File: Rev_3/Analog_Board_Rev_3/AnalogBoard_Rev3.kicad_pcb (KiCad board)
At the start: 4 copper layers, 59.5 x 114.5 mm, 56 parts, among them J1 Conn_01x06_Male, J2 Conn_01x10_Male, J3 Conn_01x06_Male, J4 Conn_01x08_Male, SW1 SW_DIP_x04, U1 OPA2134, U12 NSL-32, U13 NSL-32, U2 OPA2134, U3 OPA2134, U4 OPA2134, U5 OPA2134, U6 NSL-32, U7 NSL-32, U8 NSL-32, U9 NSL-32

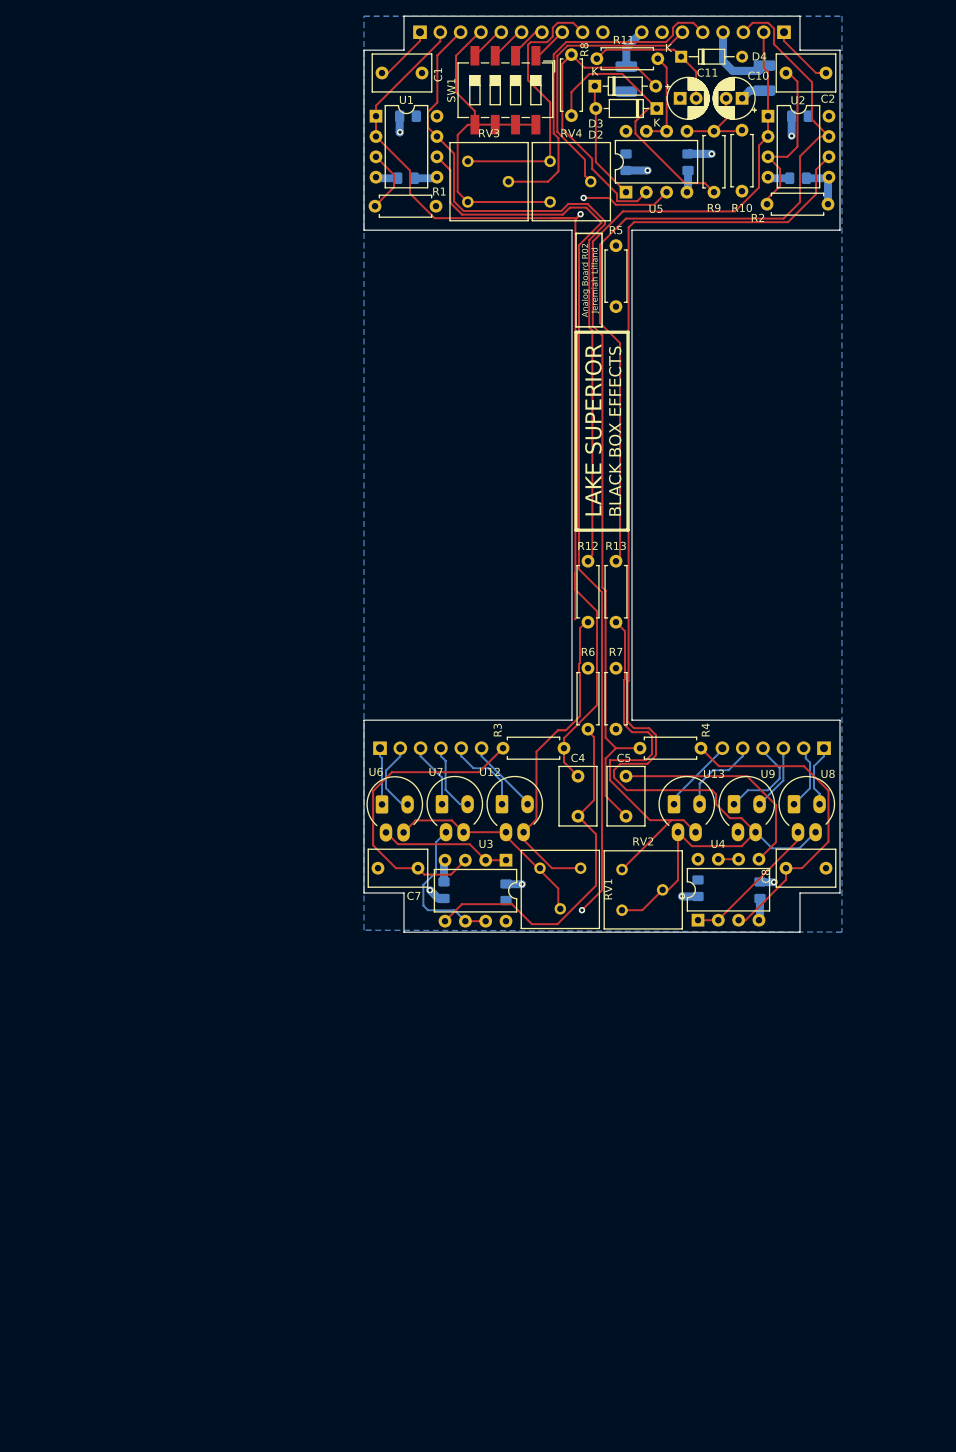
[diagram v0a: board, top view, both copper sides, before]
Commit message: Pivoting to Passive Jack Boards
Finalized layout for input/output Jack Boards, which are now completely passive and connected with board-to-board connectors. Schematics are not updated yet, just figuring out placement/dimensions.
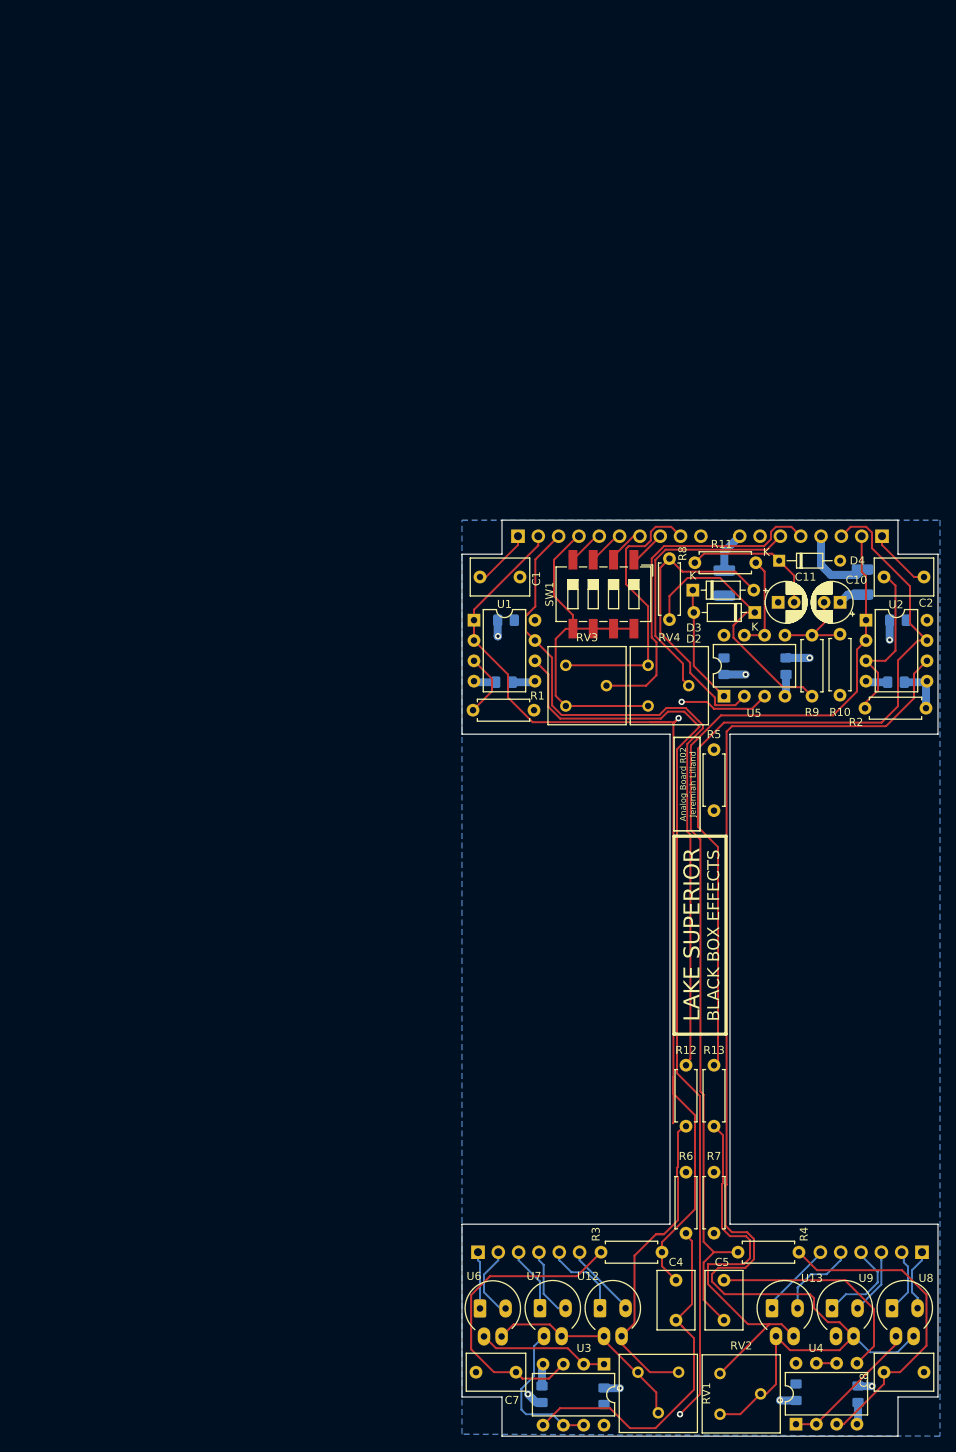
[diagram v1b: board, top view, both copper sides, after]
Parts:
- moved C10 64.2 mm to (148.3, 111.8)
- moved C11 64.2 mm to (140.5, 111.8)
- moved C12 64.2 mm to (155.2, 121.8)
- moved C13 64.2 mm to (118.8, 211.0)
- moved C14 64.2 mm to (111.0, 210.8)
- moved C15 64.2 mm to (142.8, 210.5)
- moved C16 64.2 mm to (150.5, 210.8)
- moved C17 64.2 mm to (133.8, 119.8)
- moved C18 64.2 mm to (141.5, 119.8)
- moved C19 64.2 mm to (133.8, 109.4)
- moved C3 64.2 mm to (106.5, 114.0)
- moved C4 64.2 mm to (127.8, 201.5)
- moved C5 64.2 mm to (133.8, 196.5)
- moved C6 64.2 mm to (106.2, 121.8)
- moved C7 64.2 mm to (102.8, 208.0)
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
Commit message: Added analog board back, switched to Jacks on Bottom
Added analog board mezzanine back to fit everything. Finalized decision on jack boards; jacks on bottom, wire to board connectors between jack boards and digital board. Tentative board outlines defined and scoped out component placement.
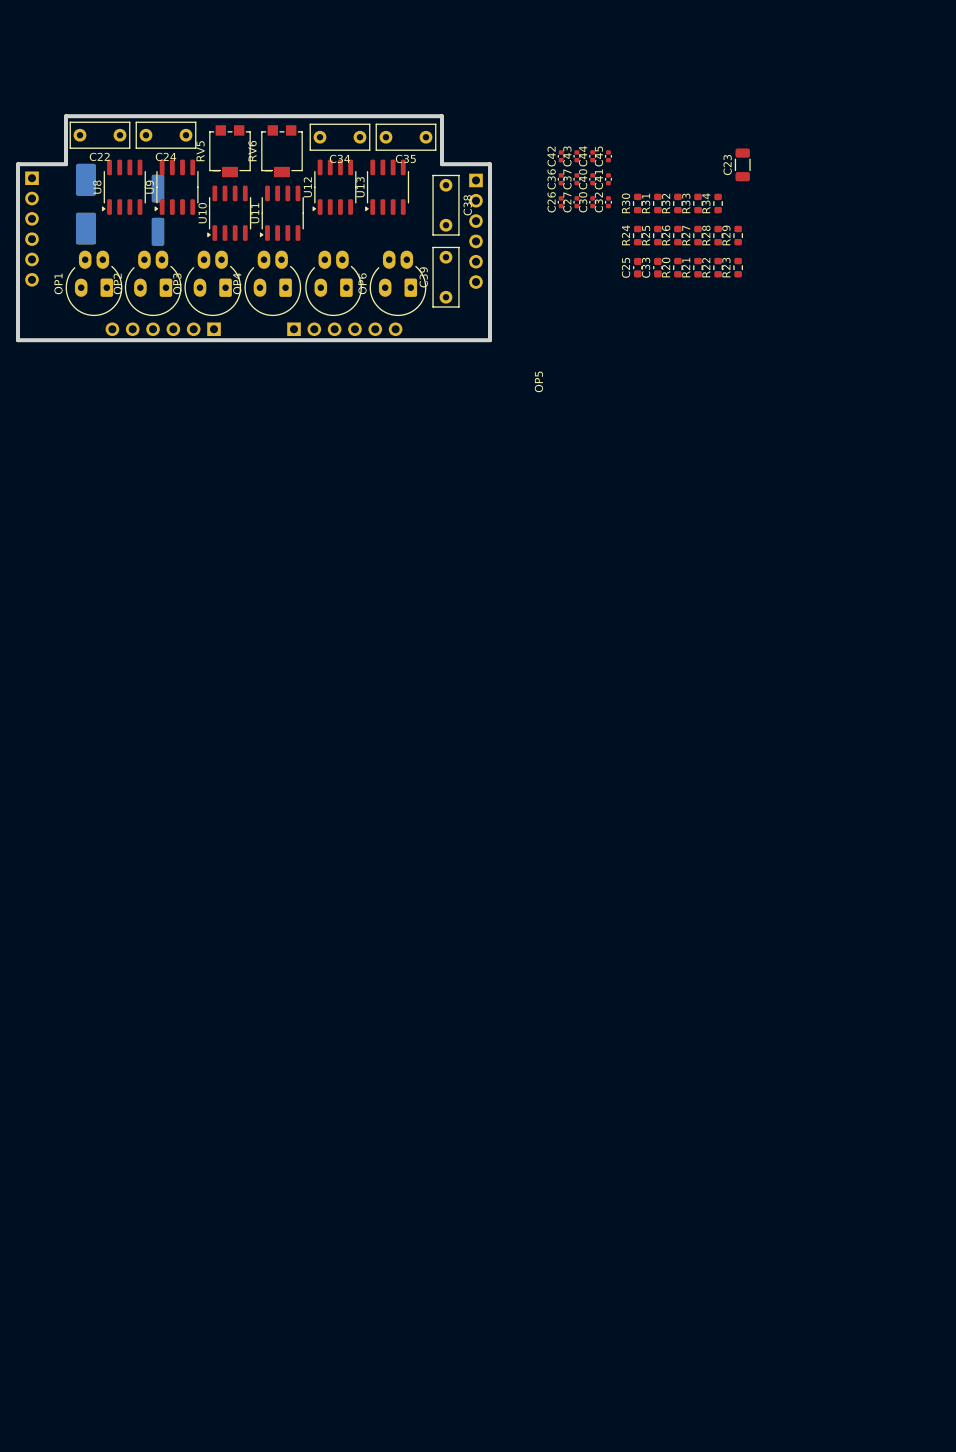
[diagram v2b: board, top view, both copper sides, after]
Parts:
- removed C1, C2: 47n, Capacitor_THT:C_Rect_L7.2mm_W4.5mm_P5.00mm_FKS2_FKP2_MKS2_MKP2
- removed C10: 4.7u, Capacitor_THT:CP_Radial_D5.0mm_P2.00mm
- removed C11: 47u, Capacitor_THT:CP_Radial_D5.0mm_P2.00mm
- removed C12, C13, C14, C15, C16, C17, C18, C3, C6, C9: 100n, Capacitor_SMD:C_0805_2012Metric_Pad1.18x1.45mm_HandSolder
- removed C19, C20: 10u, Capacitor_SMD:C_1210_3225Metric_Pad1.33x2.70mm_HandSolder
- removed C4, C5, C7, C8: 1n, Capacitor_THT:C_Rect_L7.2mm_W4.5mm_P5.00mm_FKS2_FKP2_MKS2_MKP2
- removed D2, D3: 1N914, Diode_THT:D_DO-35_SOD27_P7.62mm_Horizontal
- removed D4: D_Zener, Diode_THT:D_DO-34_SOD68_P7.62mm_Horizontal
- removed J1: Conn_01x06_Male, Connector_PinHeader_2.54mm:PinHeader_1x06_P2.54mm_Vertical
- removed J2: Conn_01x10_Male, Connector_PinHeader_2.54mm:PinHeader_1x10_P2.54mm_Vertical
- removed the J3 at (158.5, 193.0)
- removed J4: Conn_01x08_Male, Connector_PinHeader_2.54mm:PinHeader_1x08_P2.54mm_Vertical
- removed R1, R2: 1M, Resistor_THT:R_Axial_DIN0207_L6.3mm_D2.5mm_P7.62mm_Horizontal
- removed R10: 47k, Resistor_THT:R_Axial_DIN0207_L6.3mm_D2.5mm_P7.62mm_Horizontal
- removed R11, R12, R13: 1k, Resistor_THT:R_Axial_DIN0207_L6.3mm_D2.5mm_P7.62mm_Horizontal
- removed R3, R4, R6, R7: 470k, Resistor_THT:R_Axial_DIN0207_L6.3mm_D2.5mm_P7.62mm_Horizontal
- removed R5: 3.3k, Resistor_THT:R_Axial_DIN0207_L6.3mm_D2.5mm_P7.62mm_Horizontal
- removed R8: 100k, Resistor_THT:R_Axial_DIN0207_L6.3mm_D2.5mm_P7.62mm_Horizontal
- removed R9: 10k, Resistor_THT:R_Axial_DIN0207_L6.3mm_D2.5mm_P7.62mm_Horizontal
- removed RV1, RV2, RV3, RV4: 50k, Pinebox:Potentiometer_Bourns_3386F_Vertical
- removed SW1: SW_DIP_x04, Button_Switch_SMD:SW_DIP_SPSTx04_Slide_6.7x11.72mm_W8.61mm_P2.54mm_LowProfile
- removed U1, U2, U3, U4, U5: OPA2134, Package_DIP:DIP-8_W7.62mm
- removed U6, U7: NSL-32, Pinebox:Luna_NSL-32_Vertical
- added C21: 100u, Capacitor_SMD:CP_Elec_8x6.2, B.Cu at (54.0, 62.0)
- added C22: 22n, Capacitor_THT:C_Rect_L7.2mm_W3.0mm_P5.00mm_FKS2_FKP2_MKS2_MKP2, F.Cu at (58.2, 53.4)
- added C23: 10u, Capacitor_SMD:C_1206_3216Metric, F.Cu at (136.1, 57.1)
- added C24: 22n, Capacitor_THT:C_Rect_L7.2mm_W3.0mm_P5.00mm_FKS2_FKP2_MKS2_MKP2, F.Cu at (66.5, 53.4)
- added C25: 1u, Capacitor_SMD:C_0603_1608Metric, F.Cu at (123.0, 69.9)
- added C26: 22p, Capacitor_SMD:C_0402_1005Metric, F.Cu at (113.4, 61.8)
- added C27: 22p, Capacitor_SMD:C_0402_1005Metric, F.Cu at (115.4, 61.8)
- added C30: 100n, Capacitor_SMD:C_0402_1005Metric, F.Cu at (117.3, 61.8)
- added C31: 10u, Capacitor_SMD:CP_Elec_6.3x5.8, B.Cu at (63.0, 62.8)
- added C32: 100n, Capacitor_SMD:C_0402_1005Metric, F.Cu at (119.3, 61.8)
- added C33: 1u, Capacitor_SMD:C_0603_1608Metric, F.Cu at (125.5, 69.9)
- added C34: 10n, Capacitor_THT:C_Rect_L7.2mm_W3.0mm_P5.00mm_FKS2_FKP2_MKS2_MKP2, F.Cu at (88.2, 53.6)
- added C35: 10n, Capacitor_THT:C_Rect_L7.2mm_W3.0mm_P5.00mm_FKS2_FKP2_MKS2_MKP2, F.Cu at (96.5, 53.6)
- added C36: 100n, Capacitor_SMD:C_0402_1005Metric, F.Cu at (113.4, 58.9)
- added C37: 100n, Capacitor_SMD:C_0402_1005Metric, F.Cu at (115.4, 58.9)
- added C38: 10n, Capacitor_THT:C_Rect_L7.2mm_W3.0mm_P5.00mm_FKS2_FKP2_MKS2_MKP2, F.Cu at (99.0, 59.6)
- added C39: 10n, Capacitor_THT:C_Rect_L7.2mm_W3.0mm_P5.00mm_FKS2_FKP2_MKS2_MKP2, F.Cu at (99.0, 73.6)
- added C40: 100n, Capacitor_SMD:C_0402_1005Metric, F.Cu at (117.3, 58.9)
- added C41: 100n, Capacitor_SMD:C_0402_1005Metric, F.Cu at (119.3, 58.9)
- added C42: 100n, Capacitor_SMD:C_0402_1005Metric, F.Cu at (113.4, 56.0)
- added C43: 100n, Capacitor_SMD:C_0402_1005Metric, F.Cu at (115.4, 56.0)
- added C44: 100n, Capacitor_SMD:C_0402_1005Metric, F.Cu at (117.3, 56.0)
- added C45: 100n, Capacitor_SMD:C_0402_1005Metric, F.Cu at (119.3, 56.0)
- added J3: Conn_01x06_Male, Connector_PinHeader_2.54mm:PinHeader_1x06_P2.54mm_Vertical, B.Cu at (47.2, 58.8)
- added J3: Conn_01x06_Male, Connector_PinHeader_2.54mm:PinHeader_1x06_P2.54mm_Vertical, B.Cu at (102.8, 59.0)
- added J3: Conn_01x06_Male, Connector_PinHeader_2.54mm:PinHeader_1x06_P2.54mm_Vertical, B.Cu at (80.0, 77.6)
- added J3: Conn_01x06_Male, Connector_PinHeader_2.54mm:PinHeader_1x06_P2.54mm_Vertical, B.Cu at (70.0, 77.6)
- added OP1: NSL-32, g-opt:Luna_NSL-32_Vertical, F.Cu at (56.6, 72.4)
- added OP2: NSL-32, g-opt:Luna_NSL-32_Vertical, F.Cu at (64.0, 72.4)
- added OP3: NSL-32, g-opt:Luna_NSL-32_Vertical, F.Cu at (71.5, 72.4)
- added OP4: NSL-32, g-opt:Luna_NSL-32_Vertical, F.Cu at (79.0, 72.4)
- added OP5: NSL-32, g-opt:Luna_NSL-32_Vertical, F.Cu at (86.5, 72.4)
- added OP6: NSL-32, g-opt:Luna_NSL-32_Vertical, F.Cu at (94.6, 72.4)
- added R20: 1, Resistor_SMD:R_0603_1608Metric, F.Cu at (128.0, 69.9)
- added R21: 1M, Resistor_SMD:R_0603_1608Metric, F.Cu at (130.5, 69.9)
- added R22: 1M, Resistor_SMD:R_0603_1608Metric, F.Cu at (133.0, 69.9)
- added R23: 1M, Resistor_SMD:R_0603_1608Metric, F.Cu at (135.5, 69.9)
- added R24: 1M, Resistor_SMD:R_0603_1608Metric, F.Cu at (123.0, 65.9)
- added R25: 100k, Resistor_SMD:R_0603_1608Metric, F.Cu at (125.5, 65.9)
- added R26: 100k, Resistor_SMD:R_0603_1608Metric, F.Cu at (128.0, 65.9)
- added R27: 39k, Resistor_SMD:R_0603_1608Metric, F.Cu at (130.5, 65.9)
- added R28: 39k, Resistor_SMD:R_0603_1608Metric, F.Cu at (133.0, 65.9)
- added R29: 39k, Resistor_SMD:R_0603_1608Metric, F.Cu at (135.5, 65.9)
- added R30: 39k, Resistor_SMD:R_0603_1608Metric, F.Cu at (123.0, 61.9)
- added R31: 100, Resistor_SMD:R_0603_1608Metric, F.Cu at (125.5, 61.9)
- added R32: 100, Resistor_SMD:R_0603_1608Metric, F.Cu at (128.0, 61.9)
- added R33: 330, Resistor_SMD:R_0603_1608Metric, F.Cu at (130.5, 61.9)
- added R34: 330, Resistor_SMD:R_0603_1608Metric, F.Cu at (133.0, 61.9)
- added RV5: B1k, g-pot:Potentiometer_Bourns_3214G_Horizontal, F.Cu at (72.0, 55.4)
- added RV6: B1k, g-pot:Potentiometer_Bourns_3214G_Horizontal, F.Cu at (78.5, 55.4)
- added U10: OPA1688IDR, Package_SO:SOIC-8_3.9x4.9mm_P1.27mm, F.Cu at (72.0, 63.1)
- added U11: OPA1688IDR, Package_SO:SOIC-8_3.9x4.9mm_P1.27mm, F.Cu at (78.6, 63.1)
- U12, U13, U9: value NSL-32 -> OPA1688IDR; footprint Pinebox:Luna_NSL-32_Vertical -> Package_SO:SOIC-8_3.9x4.9mm_P1.27mm
- U8: value NSL-32 -> TLE2426xD; footprint Pinebox:Luna_NSL-32_Vertical -> Package_SO:SOIC-8_3.9x4.9mm_P1.27mm
- moved U8 169.8 mm to (58.9, 59.9), turned to 90 degrees
- moved U9 162.3 mm to (65.4, 59.9), turned to 90 degrees
- moved U13 148.1 mm to (91.8, 59.9), turned to 90 degrees
- moved U12 144.0 mm to (85.2, 59.9), turned to 90 degrees
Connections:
- U12 pad 1: /PWM_VOL1 -> /Analog/LP_OUT_L
- U12 pad 2: /PWM_VOL1_RTN -> /Analog/LP_OUT_L
- U12 pad 3: Net-(R12-Pad1) -> /Analog/LP_L
- U12 pad 4: /LDRA_2 -> AGND
- U13 pad 1: /PWM_VOL2 -> /Analog/EFF_R
- U13 pad 2: /PWM_VOL2_RTN -> Net-(U13A--)
- U13 pad 3: Net-(R13-Pad1) -> VREF
- U13 pad 4: /LDRC_2 -> AGND
- U8 pad 1: /PWM_3 -> VREF
- U8 pad 2: /PWM_3_RTN -> AGND
- U8 pad 3: /LDRC_2 -> VCC
- U8 pad 4: /LDRC_1 -> unconnected-(U8-NC-Pad4)
- U9 pad 1: /PWM_4 -> /Analog/BYP_L
- U9 pad 2: /PWM_4_RTN -> /Analog/BYP_L
- U9 pad 3: /LDRC_2 -> Net-(U9A-+)
- U9 pad 4: /LDRD_1 -> AGND
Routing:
- net /LDRC_2: track 162.1 -> 0.00 mm
- net /LDRA_2: track 145.7 -> 0.00 mm, vias 1 -> 0
- net /CH1_BYP: track 144.1 -> 0.00 mm, vias 2 -> 0
- net /CH2_BYP: track 121.6 -> 0.00 mm
- net /CH2_EFF: track 99.1 -> 0.00 mm
- net /CH1_EFF: track 89.2 -> 0.00 mm
- net Net-(R13-Pad1): track 49.9 -> 0.00 mm
- net Net-(D2-Pad2): track 46.1 -> 0.00 mm
- net Net-(C4-Pad1): track 44.5 -> 0.00 mm
- net GNDD: track 43.4 -> 0.00 mm
- net /TRIM_1: track 42.9 -> 0.00 mm
- net Net-(C8-Pad2): track 40.7 -> 0.00 mm
- net Net-(R12-Pad1): track 40.5 -> 0.00 mm
- net Net-(C7-Pad2): track 39.0 -> 0.00 mm
- net GND: track 35.7 -> 0.00 mm, vias 8 -> 0
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- removed copper zone on B.Cu, net +9V
- removed copper zone on In1.Cu, net -9V
- removed copper zone on In2.Cu, net GND
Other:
- board size 59.5 x 114.5 mm -> 59 x 28 mm
- board text removed: "Analog Board R02 Jeremiah Lilland"
- board text removed: "BLACK BOX EFFECTS"
- board text removed: "LAKE SUPERIOR"
